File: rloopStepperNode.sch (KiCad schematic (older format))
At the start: 0 parts

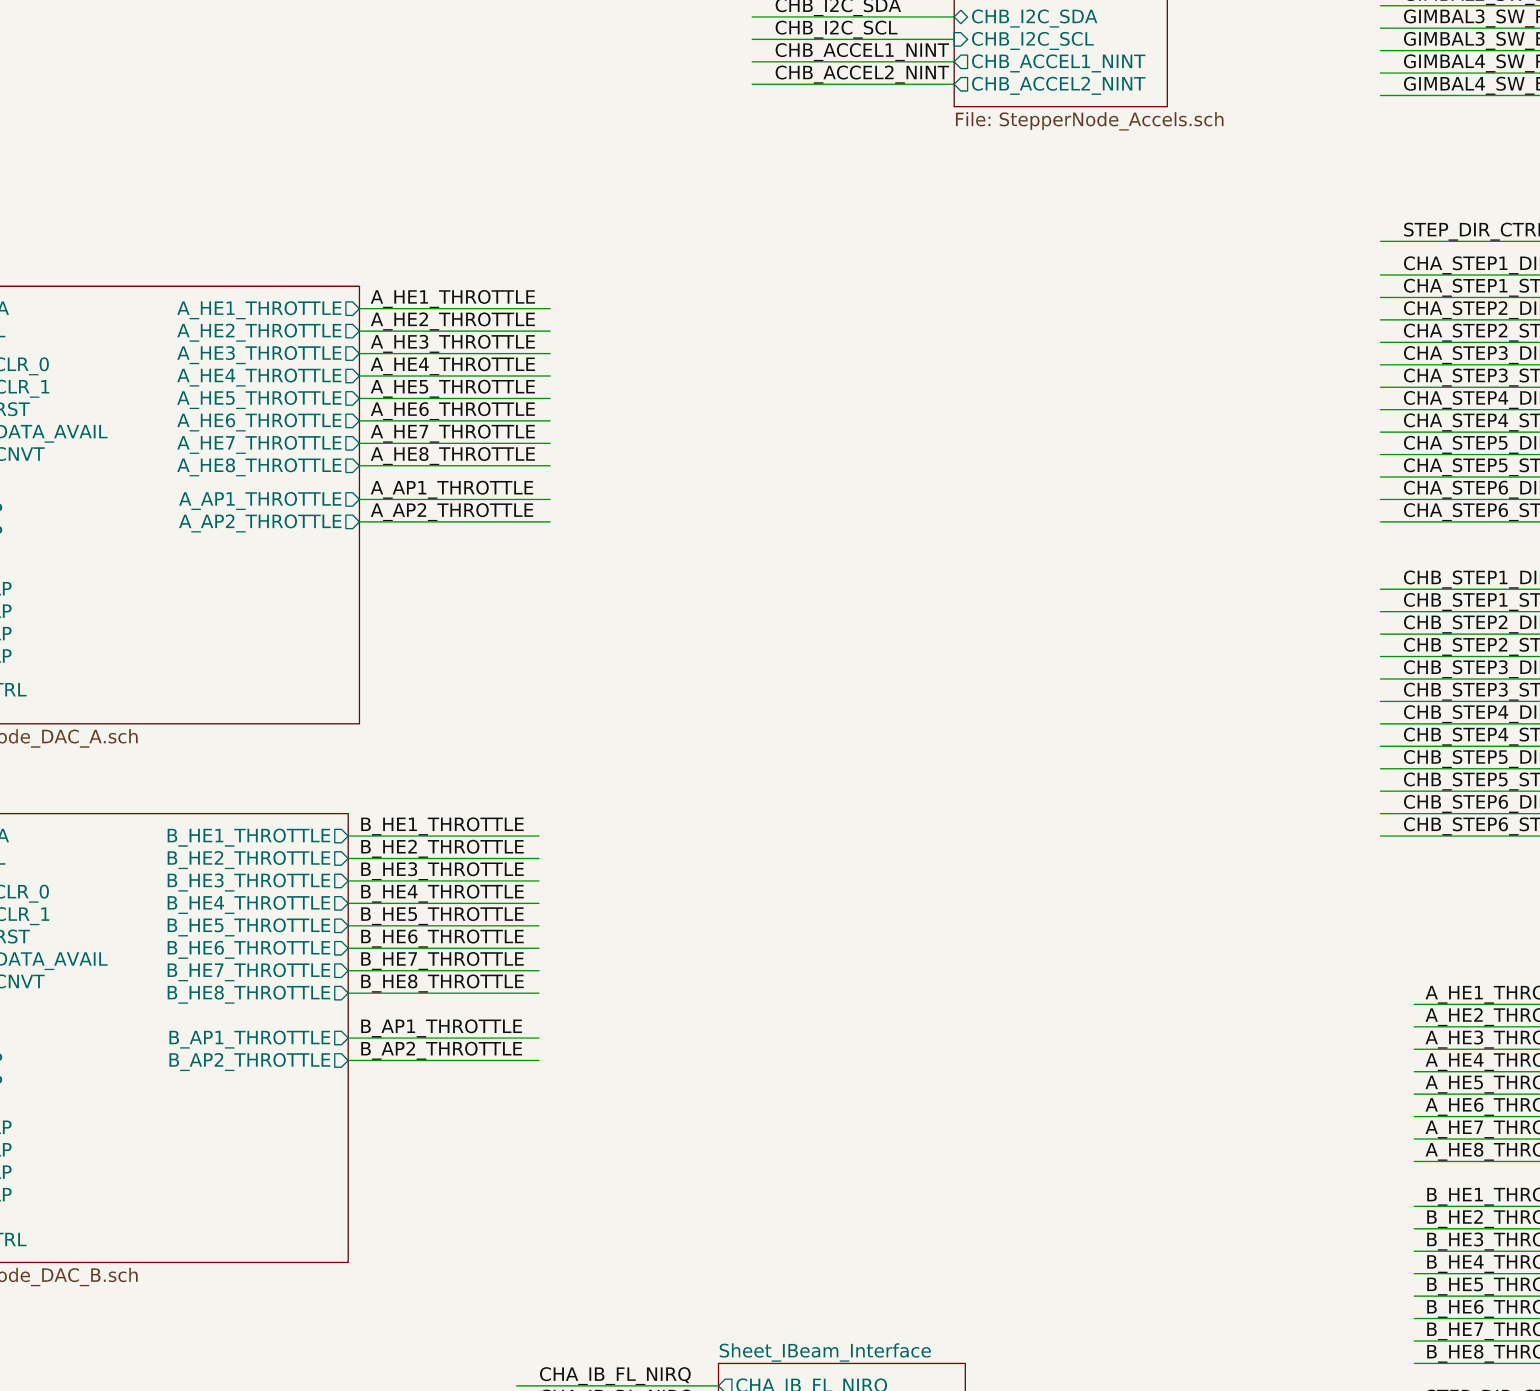
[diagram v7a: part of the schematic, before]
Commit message: Added sheet for Stepper Motor RTD temp sensors.
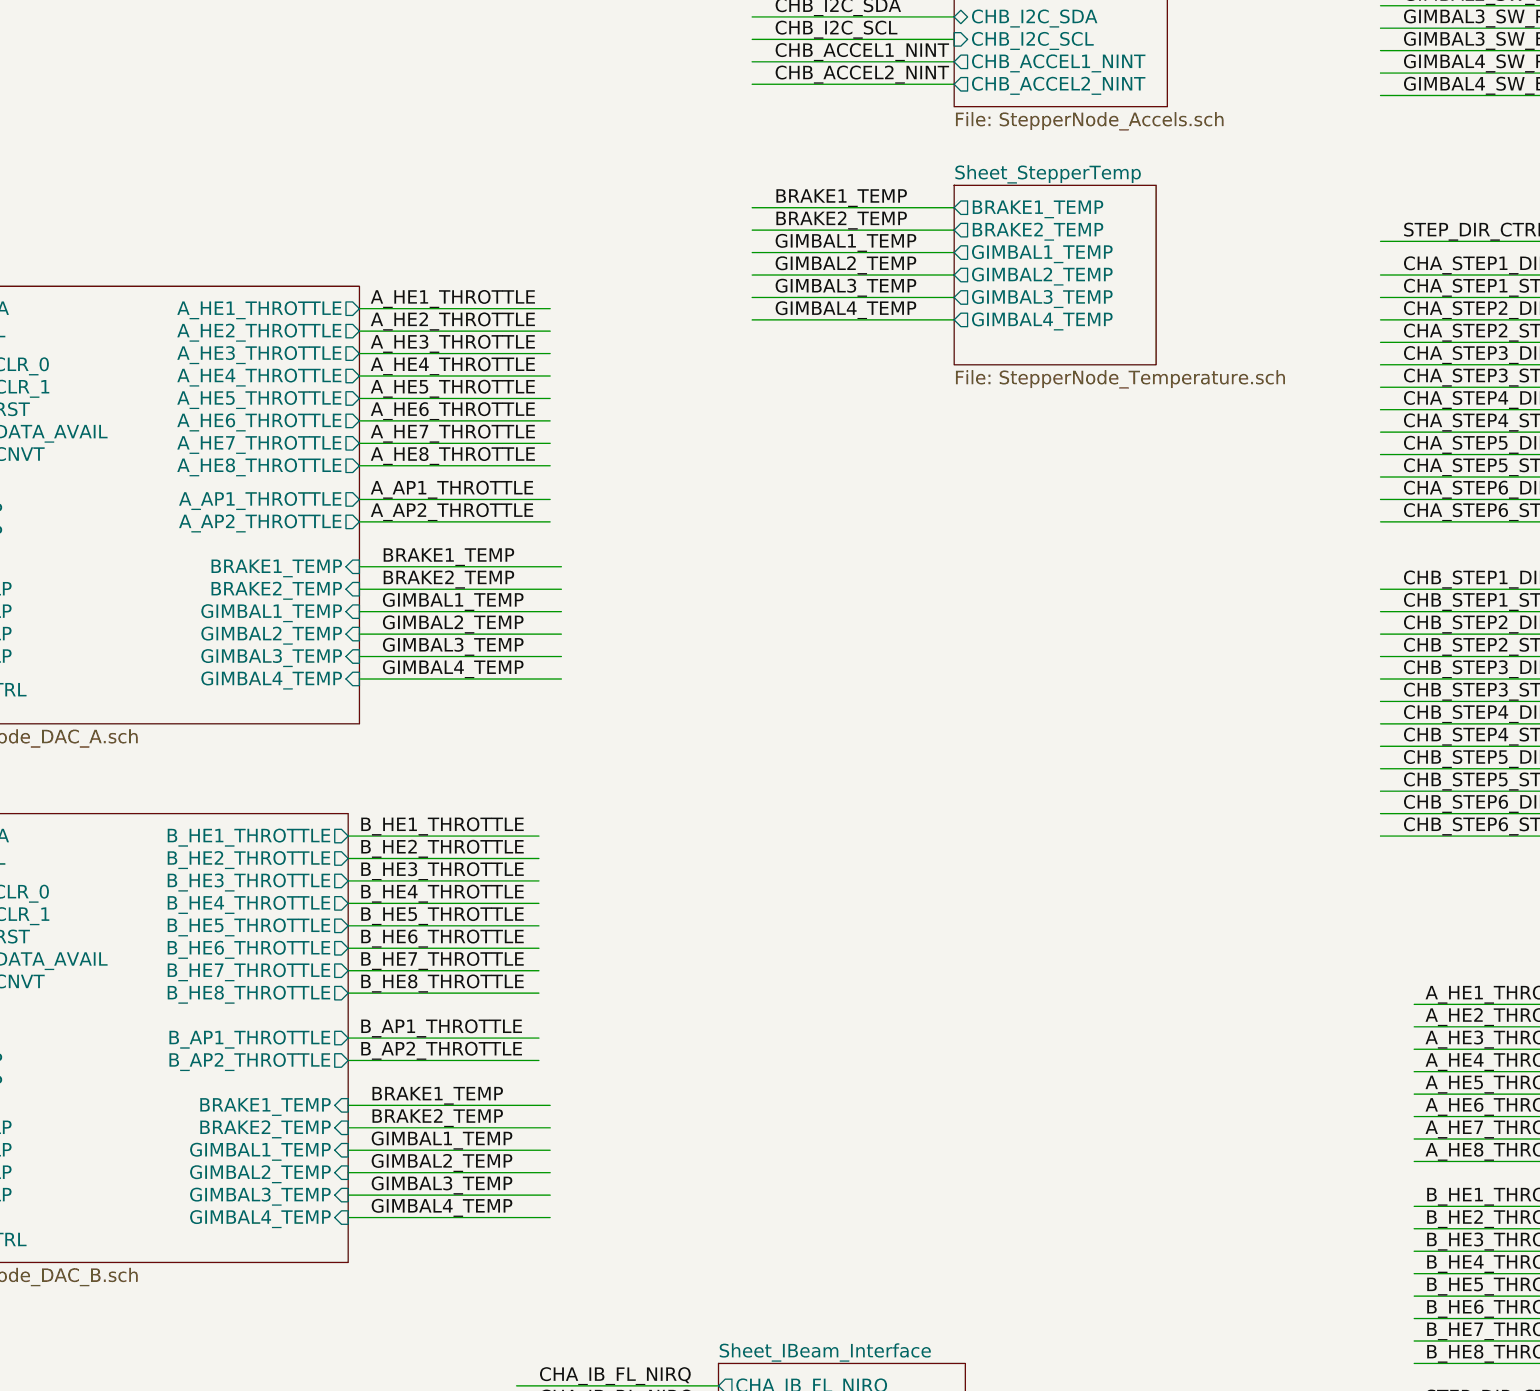
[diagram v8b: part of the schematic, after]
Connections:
- net labels added: BRAKE1_TEMP, BRAKE2_TEMP, GIMBAL1_TEMP, GIMBAL2_TEMP, GIMBAL3_TEMP, GIMBAL4_TEMP
- wire segments 214 -> 232
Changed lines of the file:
@@
 LIBS:microcontrollers
 LIBS:dsp
-LIBS:microchip
 LIBS:analog_switches
 LIBS:motorola
@@
 $Descr A3 16535 11693
 encoding utf-8
-Sheet 1 16
+Sheet 1 17
 Title "Top Level"
 Date ""
@@
 F24 "A_AP1_THROTTLE" O R 8750 4800 60
 F25 "A_AP2_THROTTLE" O R 8750 4900 60
+F26 "BRAKE1_TEMP" I R 8750 5100 60
+F27 "BRAKE2_TEMP" I R 8750 5200 60
+F28 "GIMBAL1_TEMP" I R 8750 5300 60
+F29 "GIMBAL2_TEMP" I R 8750 5400 60
+F30 "GIMBAL3_TEMP" I R 8750 5500 60
+F31 "GIMBAL4_TEMP" I R 8750 5600 60
 $EndSheet
 $Sheet
@@
 F24 "B_AP1_THROTTLE" O R 8700 7200 60
 F25 "B_AP2_THROTTLE" O R 8700 7300 60
+F26 "BRAKE1_TEMP" I R 8700 7500 60
+F27 "BRAKE2_TEMP" I R 8700 7600 60
+F28 "GIMBAL1_TEMP" I R 8700 7700 60
+F29 "GIMBAL2_TEMP" I R 8700 7800 60
+F30 "GIMBAL3_TEMP" I R 8700 7900 60
+F31 "GIMBAL4_TEMP" I R 8700 8000 60
 $EndSheet
 Wire Wire Line
@@
 Text Label 5550 1250 0    60   ~ 0
 PUSH_INTLK_A
+$Sheet
+S 11400 3400 900  800
+U 57559C15
+F0 "Sheet_StepperTemp" 60
+F1 "StepperNode_Temperature.sch" 60
+F2 "BRAKE1_TEMP" O L 11400 3500 60
+F3 "BRAKE2_TEMP" O L 11400 3600 60
+F4 "GIMBAL1_TEMP" O L 11400 3700 60
+F5 "GIMBAL2_TEMP" O L 11400 3800 60
+F6 "GIMBAL3_TEMP" O L 11400 3900 60
+F7 "GIMBAL4_TEMP" O L 11400 4000 60
+$EndSheet
+Wire Wire Line
+	10500 3500 11400 3500
+Text Label 10600 3500 0    60   ~ 0
+BRAKE1_TEMP
+Wire Wire Line
+	10500 3600 11400 3600
+Text Label 10600 3600 0    60   ~ 0
+BRAKE2_TEMP
+Wire Wire Line
+	10500 3700 11400 3700
+Text Label 10600 3700 0    60   ~ 0
+GIMBAL1_TEMP
+Wire Wire Line
+	10500 3800 11400 3800
+Text Label 10600 3800 0    60   ~ 0
+GIMBAL2_TEMP
+Wire Wire Line
+	10500 3900 11400 3900
+Text Label 10600 3900 0    60   ~ 0
+GIMBAL3_TEMP
+Wire Wire Line
+	10500 4000 11400 4000
+Text Label 10600 4000 0    60   ~ 0
+GIMBAL4_TEMP
+Wire Wire Line
+	8750 5100 9650 5100
+Text Label 8850 5100 0    60   ~ 0
+BRAKE1_TEMP
+Wire Wire Line
+	8750 5200 9650 5200
+Text Label 8850 5200 0    60   ~ 0
+BRAKE2_TEMP
+Wire Wire Line
+	8750 5300 9650 5300
+Text Label 8850 5300 0    60   ~ 0
+GIMBAL1_TEMP
+Wire Wire Line
+	8750 5400 9650 5400
+Text Label 8850 5400 0    60   ~ 0
+GIMBAL2_TEMP
+Wire Wire Line
+	8750 5500 9650 5500
+Text Label 8850 5500 0    60   ~ 0
+GIMBAL3_TEMP
+Wire Wire Line
+	8750 5600 9650 5600
+Text Label 8850 5600 0    60   ~ 0
+GIMBAL4_TEMP
+Wire Wire Line
+	8700 7500 9600 7500
+Text Label 8800 7500 0    60   ~ 0
+BRAKE1_TEMP
+Wire Wire Line
+	8700 7600 9600 7600
+Text Label 8800 7600 0    60   ~ 0
+BRAKE2_TEMP
+Wire Wire Line
+	8700 7700 9600 7700
+Text Label 8800 7700 0    60   ~ 0
+GIMBAL1_TEMP
+Wire Wire Line
+	8700 7800 9600 7800
+Text Label 8800 7800 0    60   ~ 0
+GIMBAL2_TEMP
+Wire Wire Line
+	8700 7900 9600 7900
+Text Label 8800 7900 0    60   ~ 0
+GIMBAL3_TEMP
+Wire Wire Line
+	8700 8000 9600 8000
+Text Label 8800 8000 0    60   ~ 0
+GIMBAL4_TEMP
 $EndSCHEMATC
